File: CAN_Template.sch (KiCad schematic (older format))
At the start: 18 parts, among them U1 MCP2515-xSO, U2 SN65HVD1050D

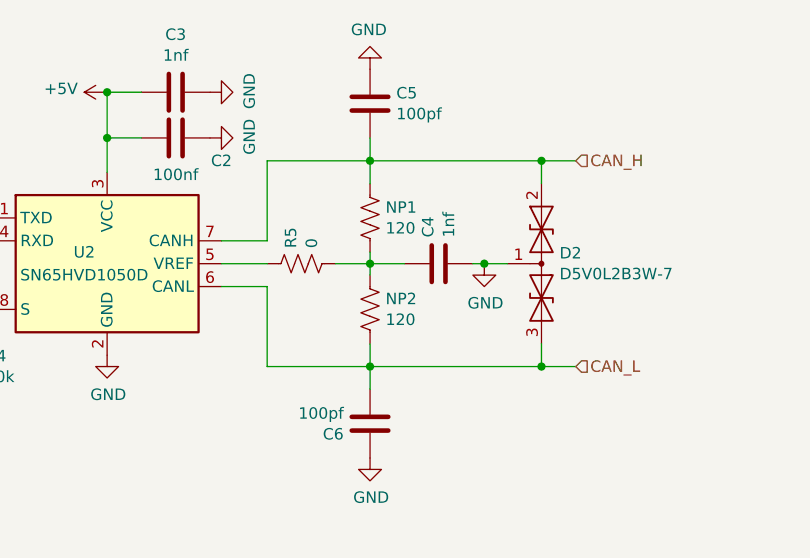
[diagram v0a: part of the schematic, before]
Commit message: Fixed CAN termination
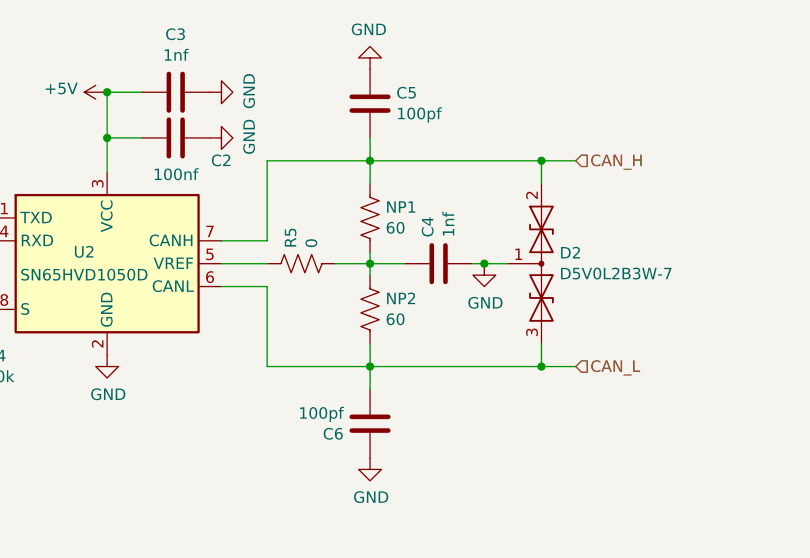
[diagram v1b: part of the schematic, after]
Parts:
- NP1, NP2: value 120 -> 60
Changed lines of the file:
@@
 P 6600 3250
 F 0 "NP1" H 6668 3296 50  0000 L CNN
-F 1 "120" H 6668 3205 50  0000 L CNN
+F 1 "60" H 6668 3205 50  0000 L CNN
 F 2 "Resistor_SMD:R_0805_2012Metric_Pad1.15x1.40mm_HandSolder" V 6640 3240 50  0001 C CNN
 F 3 "~" H 6600 3250 50  0001 C CNN
@@
 P 6600 3650
 F 0 "NP2" H 6668 3696 50  0000 L CNN
-F 1 "120" H 6668 3605 50  0000 L CNN
+F 1 "60" H 6668 3605 50  0000 L CNN
 F 2 "Resistor_SMD:R_0805_2012Metric_Pad1.15x1.40mm_HandSolder" V 6640 3640 50  0001 C CNN
 F 3 "~" H 6600 3650 50  0001 C CNN

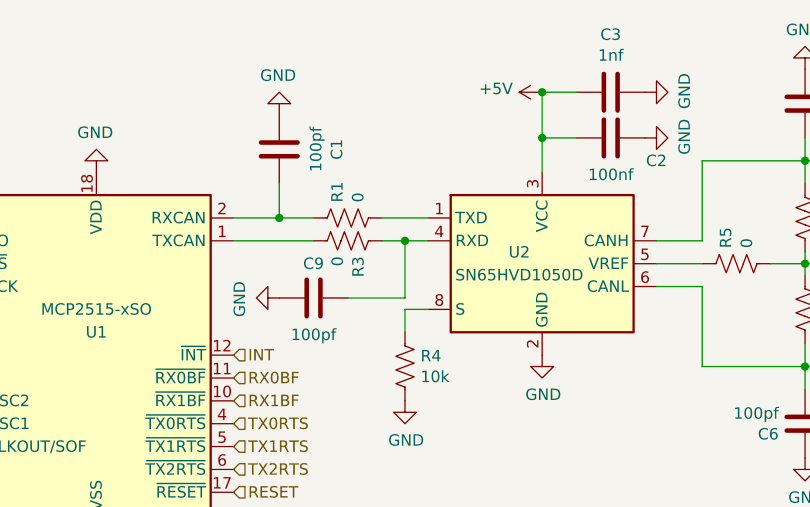
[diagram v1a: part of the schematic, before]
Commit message: Fixed CAN
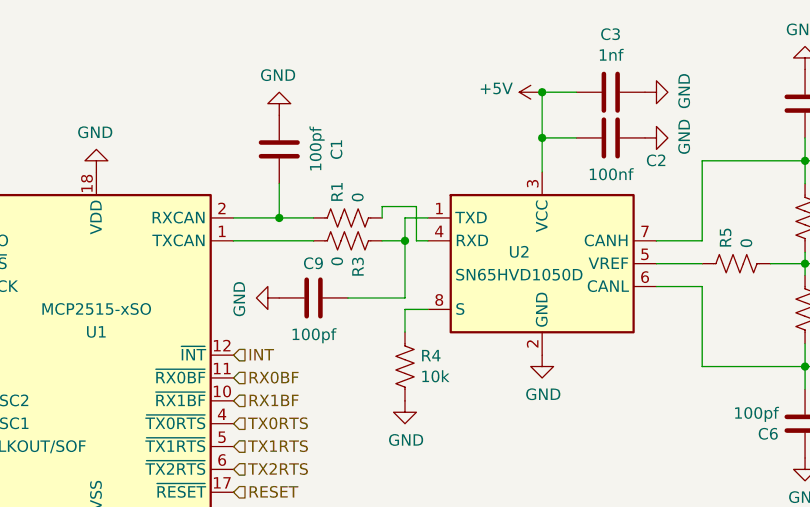
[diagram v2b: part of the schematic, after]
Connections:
- net at U2.1 (TXD): now also C9.2, R3.1; no longer R1.2
- new net: R1.2, U2.4 (RXD)
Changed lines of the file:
@@
 EESchema Schematic File Version 4
-LIBS:CAN_Template-cache
 EELAYER 30 0
 EELAYER END
@@
 Wire Wire Line
 	4850 3600 4850 3350
-Connection ~ 4850 3350
-Wire Wire Line
-	4850 3350 4950 3350
 Wire Wire Line
 	4300 3100 4300 3250
@@
 Wire Wire Line
 	4300 3250 4450 3250
-Wire Wire Line
-	4750 3250 4950 3250
 NoConn ~ 2900 4050
 NoConn ~ 2900 4150
@@
 Text Label 7500 7500 0    50   ~ 0
 CAN_Transciever
+Wire Wire Line
+	4850 3350 4850 3250
+Wire Wire Line
+	4850 3250 4950 3250
+Connection ~ 4850 3350
+Wire Wire Line
+	4750 3250 4750 3200
+Wire Wire Line
+	4750 3200 4900 3200
+Wire Wire Line
+	4900 3200 4900 3350
+Wire Wire Line
+	4900 3350 4950 3350
 $EndSCHEMATC
